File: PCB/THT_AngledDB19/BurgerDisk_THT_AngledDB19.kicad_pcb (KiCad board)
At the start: 2 copper layers, 93.7 x 73.4 mm, 18 parts, among them J1 Daisy port in, J2 MicroSD module, J3 UART, J4 Daisy port out, U1 PC817

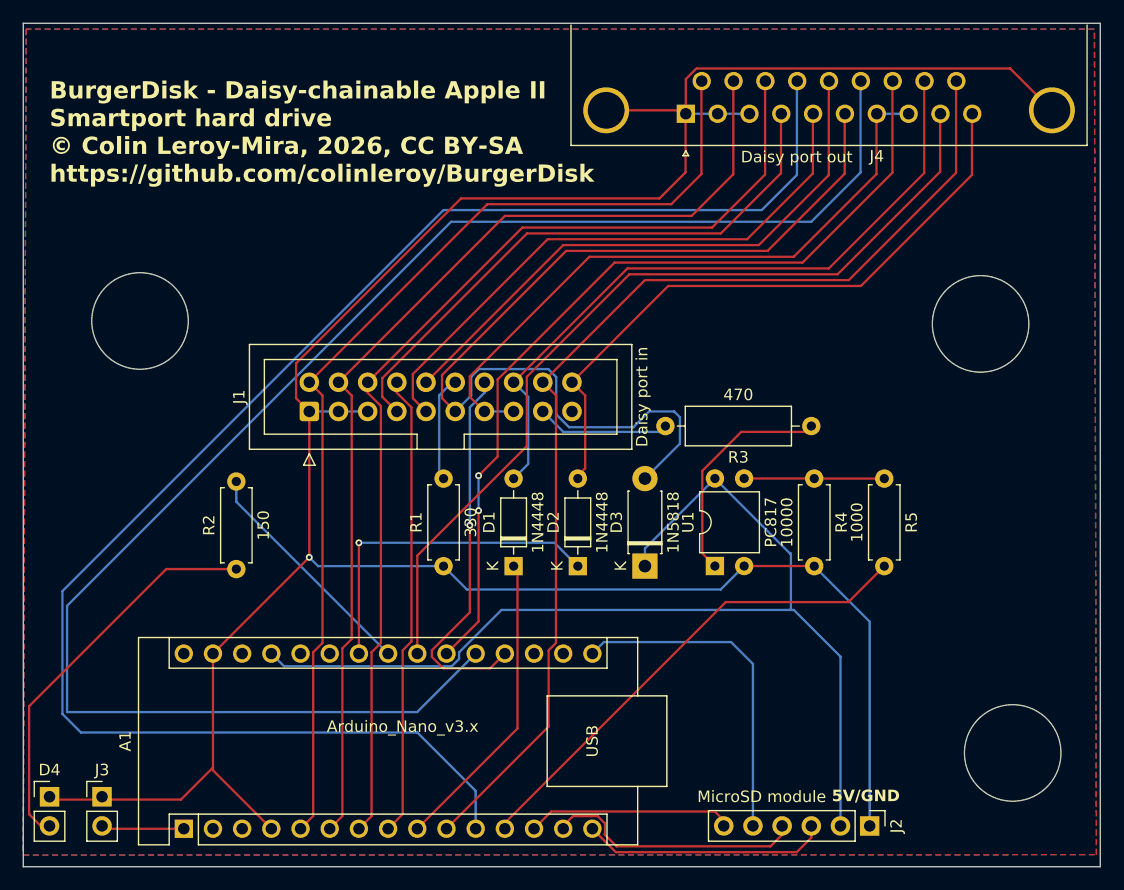
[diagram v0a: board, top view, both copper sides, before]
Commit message: Wider tracks for power
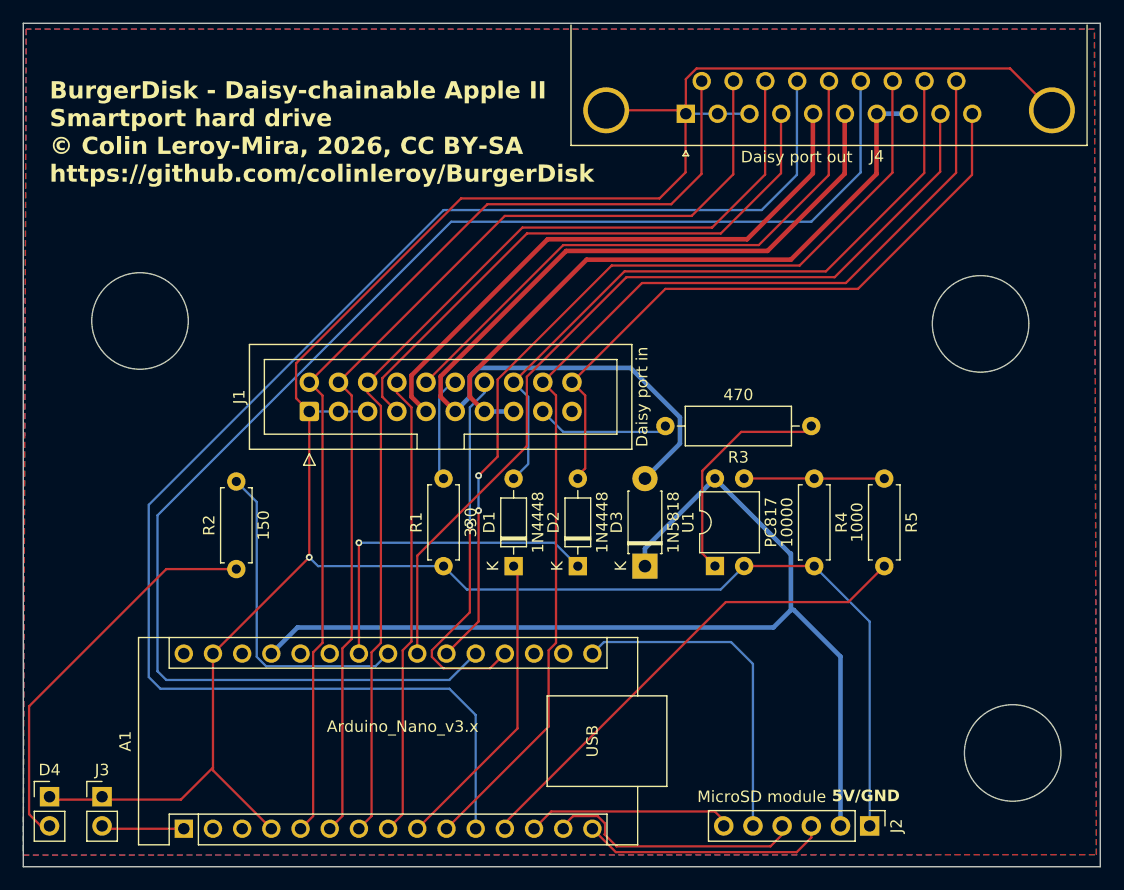
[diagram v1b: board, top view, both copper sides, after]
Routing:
- net HDSEL_out: track 139.6 -> 124.0 mm
- net PH3_out: track 139.8 -> 131.2 mm
- net Net-(A1-A4): track 20.4 -> 28.2 mm
- net 5V_apple2: track 84.6 -> 81.8 mm
- net 5V_burgerDisk: track 93.1 -> 91.9 mm

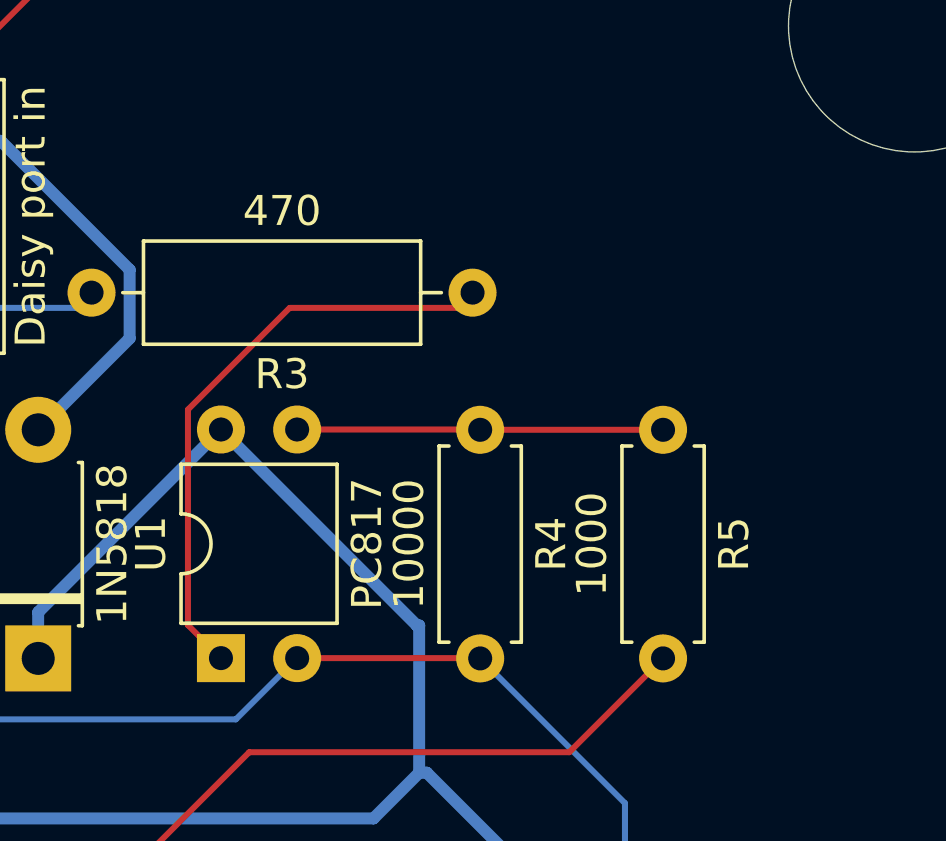
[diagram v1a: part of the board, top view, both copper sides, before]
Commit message: Reverse 3 resistors for correct silkscreen orientation
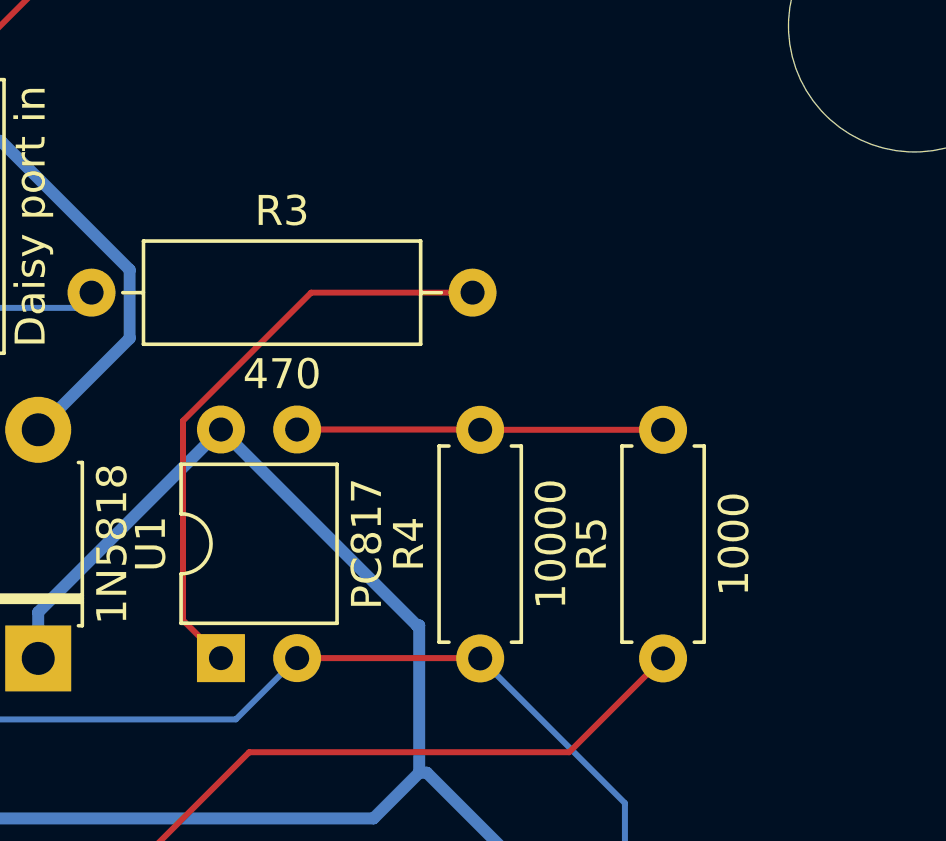
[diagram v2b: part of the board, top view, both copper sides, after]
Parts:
- moved R3 12.7 mm to (126.7, 72.9), turned to 0 degrees
- moved R4 7.62 mm to (139.7, 85.1), turned to 90 degrees
- moved R5 7.62 mm to (145.8, 85.1), turned to 90 degrees
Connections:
- R3 pad 1: Net-(R3-Pad1) -> DRV2_in
- R3 pad 2: DRV2_in -> Net-(R3-Pad2)
- R4 pad 1: Net-(R4-Pad1) -> GND
- R4 pad 2: GND -> Net-(R4-Pad2)
- R5 pad 1: Net-(R4-Pad1) -> DRV2_burgerDisk
- R5 pad 2: DRV2_burgerDisk -> Net-(R4-Pad2)
- U1 pad 1: Net-(R3-Pad1) -> Net-(R3-Pad2)
- U1 pad 3: Net-(R4-Pad1) -> Net-(R4-Pad2)
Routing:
- net Net-(R3-Pad2): track 0.00 -> 19.9 mm
- net Net-(R3-Pad1): track 19.8 -> 0.00 mm
- net Net-(R4-Pad2): track 0.00 -> 12.2 mm
- net Net-(R4-Pad1): track 12.2 -> 0.00 mm
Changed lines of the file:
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@@
   (net 36 "unconnected-(A1-A6-Pad25)")
   (net 37 "unconnected-(A1-3V3-Pad17)")
-  (net 38 "Net-(R4-Pad1)")
-  (net 39 "Net-(R3-Pad1)")
+  (net 38 "Net-(R3-Pad2)")
+  (net 39 "Net-(R4-Pad2)")
   (net 40 "HDSEL_in")
   (net 41 "Net-(D4-A)")
@@
       (stroke (width 0.1) (type solid)) (layer "F.Fab"))
     (pad "1" thru_hole rect (at 0 0 90) (size 1.6 1.6) (drill 0.8) (layers "*.Cu" "*.Mask")
-      (net 39 "Net-(R3-Pad1)") (pintype "passive"))
+      (net 38 "Net-(R3-Pad2)") (pintype "passive"))
     (pad "2" thru_hole oval (at 0 2.54 90) (size 1.6 1.6) (drill 0.8) (layers "*.Cu" "*.Mask")
       (net 2 "GND") (pintype "passive"))
     (pad "3" thru_hole oval (at 7.62 2.54 90) (size 1.6 1.6) (drill 0.8) (layers "*.Cu" "*.Mask")
-      (net 38 "Net-(R4-Pad1)") (pintype "passive"))
+      (net 39 "Net-(R4-Pad2)") (pintype "passive"))
     (pad "4" thru_hole oval (at 7.62 0 90) (size 1.6 1.6) (drill 0.8) (layers "*.Cu" "*.Mask")
       (net 20 "5V_burgerDisk") (pintype "passive"))
@@
   )
   (footprint "Resistor_THT:R_Axial_DIN0309_L9.0mm_D3.2mm_P12.70mm_Horizontal" (layer "F.Cu")
-    (at 139.446 72.898 180)
+    (at 126.746 72.898)
     (descr "Resistor, Axial_DIN0309 series, Axial, Horizontal, pin pitch=12.7mm, 0.5W = 1/2W, length*diameter=9*3.2mm^2, http://cdn-reichelt.de/documents/datenblatt/B400/1_4W%23YAG.pdf")
     (tags "Resistor Axial_DIN0309 series Axial Horizontal pin pitch 12.7mm 0.5W = 1/2W length 9mm diameter 3.2mm")
@@
     (fp_line (start 12.7 0) (end 10.85 0)
       (stroke (width 0.1) (type solid)) (layer "F.Fab"))
-    (pad "1" thru_hole circle (at 0 0 180) (size 1.6 1.6) (drill 0.8) (layers "*.Cu" "*.Mask")
-      (net 39 "Net-(R3-Pad1)") (pintype "passive"))
-    (pad "2" thru_hole oval (at 12.7 0 180) (size 1.6 1.6) (drill 0.8) (layers "*.Cu" "*.Mask")
+    (pad "1" thru_hole circle (at 0 0) (size 1.6 1.6) (drill 0.8) (layers "*.Cu" "*.Mask")
       (net 27 "DRV2_in") (pintype "passive"))
+    (pad "2" thru_hole oval (at 12.7 0) (size 1.6 1.6) (drill 0.8) (layers "*.Cu" "*.Mask")
+      (net 38 "Net-(R3-Pad2)") (pintype "passive"))
     (model "${KICAD6_3DMODEL_DIR}/Resistor_THT.3dshapes/R_Axial_DIN0309_L9.0mm_D3.2mm_P12.70mm_Horizontal.wrl"
       (offset (xyz 0 0 0))
@@
   )
   (footprint "Resistor_THT:R_Axial_DIN0207_L6.3mm_D2.5mm_P7.62mm_Horizontal" (layer "F.Cu")
-    (at 139.7 77.47 -90)
+    (at 139.7 85.09 90)
     (descr "Resistor, Axial_DIN0207 series, Axial, Horizontal, pin pitch=7.62mm, 0.25W = 1/4W, length*diameter=6.3*2.5mm^2, http://cdn-reichelt.de/documents/datenblatt/B400/1_4W%23YAG.pdf")
     (tags "Resistor Axial_DIN0207 series Axial Horizontal pin pitch 7.62mm 0.25W = 1/4W length 6.3mm diameter 2.5mm")
@@
     (fp_line (start 7.62 0) (end 6.96 0)
       (stroke (width 0.1) (type solid)) (layer "F.Fab"))
-    (pad "1" thru_hole circle (at 0 0 270) (size 1.6 1.6) (drill 0.8) (layers "*.Cu" "*.Mask")
-      (net 38 "Net-(R4-Pad1)") (pintype "passive"))
-    (pad "2" thru_hole oval (at 7.62 0 270) (size 1.6 1.6) (drill 0.8) (layers "*.Cu" "*.Mask")
+    (pad "1" thru_hole circle (at 0 0 90) (size 1.6 1.6) (drill 0.8) (layers "*.Cu" "*.Mask")
       (net 2 "GND") (pintype "passive"))
+    (pad "2" thru_hole oval (at 7.62 0 90) (size 1.6 1.6) (drill 0.8) (layers "*.Cu" "*.Mask")
+      (net 39 "Net-(R4-Pad2)") (pintype "passive"))
     (model "${KICAD6_3DMODEL_DIR}/Resistor_THT.3dshapes/R_Axial_DIN0207_L6.3mm_D2.5mm_P7.62mm_Horizontal.wrl"
       (offset (xyz 0 0 0))
@@
   )
   (footprint "Resistor_THT:R_Axial_DIN0207_L6.3mm_D2.5mm_P7.62mm_Horizontal" (layer "F.Cu")
-    (at 145.796 77.47 -90)
+    (at 145.796 85.09 90)
     (descr "Resistor, Axial_DIN0207 series, Axial, Horizontal, pin pitch=7.62mm, 0.25W = 1/4W, length*diameter=6.3*2.5mm^2, http://cdn-reichelt.de/documents/datenblatt/B400/1_4W%23YAG.pdf")
     (tags "Resistor Axial_DIN0207 series Axial Horizontal pin pitch 7.62mm 0.25W = 1/4W length 6.3mm diameter 2.5mm")
@@
     (fp_line (start 7.62 0) (end 6.96 0)
       (stroke (width 0.1) (type solid)) (layer "F.Fab"))
-    (pad "1" thru_hole circle (at 0 0 270) (size 1.6 1.6) (drill 0.8) (layers "*.Cu" "*.Mask")
-      (net 38 "Net-(R4-Pad1)") (pintype "passive"))
-    (pad "2" thru_hole oval (at 7.62 0 270) (size 1.6 1.6) (drill 0.8) (layers "*.Cu" "*.Mask")
+    (pad "1" thru_hole circle (at 0 0 90) (size 1.6 1.6) (drill 0.8) (layers "*.Cu" "*.Mask")
       (net 10 "DRV2_burgerDisk") (pintype "passive"))
+    (pad "2" thru_hole oval (at 7.62 0 90) (size 1.6 1.6) (drill 0.8) (layers "*.Cu" "*.Mask")
+      (net 39 "Net-(R4-Pad2)") (pintype "passive"))
     (model "${KICAD6_3DMODEL_DIR}/Resistor_THT.3dshapes/R_Axial_DIN0207_L6.3mm_D2.5mm_P7.62mm_Horizontal.wrl"
       (offset (xyz 0 0 0))
@@
   (segment (start 77.973 107.945) (end 84.831 107.945) (width 0.2) (layer "F.Cu") (net 1))
   (segment (start 84.831 107.945) (end 84.836 107.94) (width 0.2) (layer "F.Cu") (net 1))
-  (segment (start 139.69 85.08) (end 139.7 85.09) (width 0.2) (layer "F.Cu") (net 2))
   (segment (start 128.524 45.72) (end 128.524 42.709365) (width 0.2) (layer "F.Cu") (net 2))
   (segment (start 121.594 45.42) (end 128.224 45.42) (width 0.2) (layer "F.Cu") (net 2))
@@
   (segment (start 95.758 71.628) (end 95.758 84.318) (width 0.2) (layer "F.Cu") (net 2))
   (segment (start 77.724 105.156) (end 77.973 105.405) (width 0.2) (layer "F.Cu") (net 2))
+  (segment (start 133.599 85.08) (end 139.69 85.08) (width 0.2) (layer "F.Cu") (net 2))
   (segment (start 77.973 105.405) (end 84.587 105.405) (width 0.2) (layer "F.Cu") (net 2))
   (segment (start 95.758 71.628) (end 94.608 70.478) (width 0.2) (layer "F.Cu") (net 2))
@@
   (segment (start 128.224 45.42) (end 128.524 45.72) (width 0.2) (layer "F.Cu") (net 2))
   (segment (start 84.587 105.405) (end 87.376 102.616) (width 0.2) (layer "F.Cu") (net 2))
+  (segment (start 139.69 85.08) (end 139.7 85.09) (width 0.2) (layer "F.Cu") (net 2))
   (segment (start 128.524 42.709365) (end 129.453365 41.78) (width 0.2) (layer "F.Cu") (net 2))
   (segment (start 128.5 50.824) (end 128.5 45.744) (width 0.2) (layer "F.Cu") (net 2))
-  (segment (start 133.599 85.08) (end 139.69 85.08) (width 0.2) (layer "F.Cu") (net 2))
   (segment (start 108.966 53.086) (end 126.238 53.086) (width 0.2) (layer "F.Cu") (net 2))
   (segment (start 126.238 53.086) (end 128.5 50.824) (width 0.2) (layer "F.Cu") (net 2))
@@
   (segment (start 131.294 45.72) (end 134.064 45.72) (width 0.2) (layer "B.Cu") (net 2))
   (segment (start 107.442 85.09) (end 109.474 87.122) (width 0.2) (layer "B.Cu") (net 2))
+  (segment (start 144.526 89.916) (end 139.7 85.09) (width 0.2) (layer "B.Cu") (net 2))
+  (segment (start 144.526 107.696) (end 144.526 89.916) (width 0.2) (layer "B.Cu") (net 2))
   (segment (start 98.298 71.628) (end 95.758 71.628) (width 0.2) (layer "B.Cu") (net 2))
-  (segment (start 144.526 89.916) (end 139.7 85.09) (width 0.2) (layer "B.Cu") (net 2))
   (segment (start 107.442 85.09) (end 96.52 85.09) (width 0.2) (layer "B.Cu") (net 2))
   (segment (start 96.52 85.09) (end 95.753 84.323) (width 0.2) (layer "B.Cu") (net 2))
-  (segment (start 144.526 107.696) (end 144.526 89.916) (width 0.2) (layer "B.Cu") (net 2))
   (segment (start 98.298 71.628) (end 100.838 71.628) (width 0.2) (layer "B.Cu") (net 2))
   (segment (start 131.557 87.122) (end 133.599 85.08) (width 0.2) (layer "B.Cu") (net 2))
@@
   (segment (start 135.128 54.102) (end 138.195 51.035) (width 0.2) (layer "B.Cu") (net 9))
   (segment (start 81.788 79.756) (end 107.442 54.102) (width 0.2) (layer "B.Cu") (net 9))
+  (segment (start 132.001 88.217) (end 142.669 88.217) (width 0.2) (layer "F.Cu") (net 10))
   (segment (start 112.776 107.442) (end 132.001 88.217) (width 0.2) (layer "F.Cu") (net 10))
-  (segment (start 132.001 88.217) (end 142.669 88.217) (width 0.2) (layer "F.Cu") (net 10))
   (segment (start 112.776 107.94) (end 112.776 107.442) (width 0.2) (layer "F.Cu") (net 10))
   (segment (start 142.669 88.217) (end 145.796 85.09) (width 0.2) (layer "F.Cu") (net 10))
@@
   (segment (start 105.918 69.088) (end 117.856 57.15) (width 0.2) (layer "F.Cu") (net 28))
   (segment (start 134.874 57.15) (end 140.965 51.059) (width 0.2) (layer "F.Cu") (net 28))
-  (segment (start 139.69 77.46) (end 139.7 77.47) (width 0.2) (layer "F.Cu") (net 38))
-  (segment (start 139.7 77.47) (end 145.796 77.47) (width 0.2) (layer "F.Cu") (net 38))
-  (segment (start 133.599 77.46) (end 139.69 77.46) (width 0.2) (layer "F.Cu") (net 38))
-  (segment (start 129.959 83.98) (end 129.959 76.797) (width 0.2) (layer "F.Cu") (net 39))
-  (segment (start 131.059 85.08) (end 129.959 83.98) (width 0.2) (layer "F.Cu") (net 39))
-  (segment (start 138.938 73.406) (end 139.446 72.898) (width 0.2) (layer "F.Cu") (net 39))
-  (segment (start 129.959 76.797) (end 133.35 73.406) (width 0.2) (layer "F.Cu") (net 39))
-  (segment (start 133.35 73.406) (end 138.938 73.406) (width 0.2) (layer "F.Cu") (net 39))
+  (segment (start 129.794 83.815) (end 131.059 85.08) (width 0.2) (layer "F.Cu") (net 38))
+  (segment (start 139.446 72.898) (end 134.065365 72.898) (width 0.2) (layer "F.Cu") (net 38))
+  (segment (start 134.065365 72.898) (end 129.794 77.169365) (width 0.2) (layer "F.Cu") (net 38))
+  (segment (start 129.794 77.169365) (end 129.794 83.815) (width 0.2) (layer "F.Cu") (net 38))
+  (segment (start 139.69 77.46) (end 139.7 77.47) (width 0.2) (layer "F.Cu") (net 39))
+  (segment (start 139.7 77.47) (end 145.796 77.47) (width 0.2) (layer "F.Cu") (net 39))
+  (segment (start 133.599 77.46) (end 139.69 77.46) (width 0.2) (layer "F.Cu") (net 39))
   (segment (start 108.458 68.834) (end 107.068 70.224) (width 0.2) (layer "B.Cu") (net 40))
   (segment (start 107.068 77.35) (end 107.442 77.724) (width 0.2) (layer "B.Cu") (net 40))
@@
     (connect_pads (clearance 0.5))
     (min_thickness 0.25) (filled_areas_thickness no)
-    (fill yes (thermal_gap 0.5) (thermal_bridge_width 0.5))
+    (fill (thermal_gap 0.5) (thermal_bridge_width 0.5))
     (polygon
       (pts
